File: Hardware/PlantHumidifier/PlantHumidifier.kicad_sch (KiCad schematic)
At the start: 9 parts

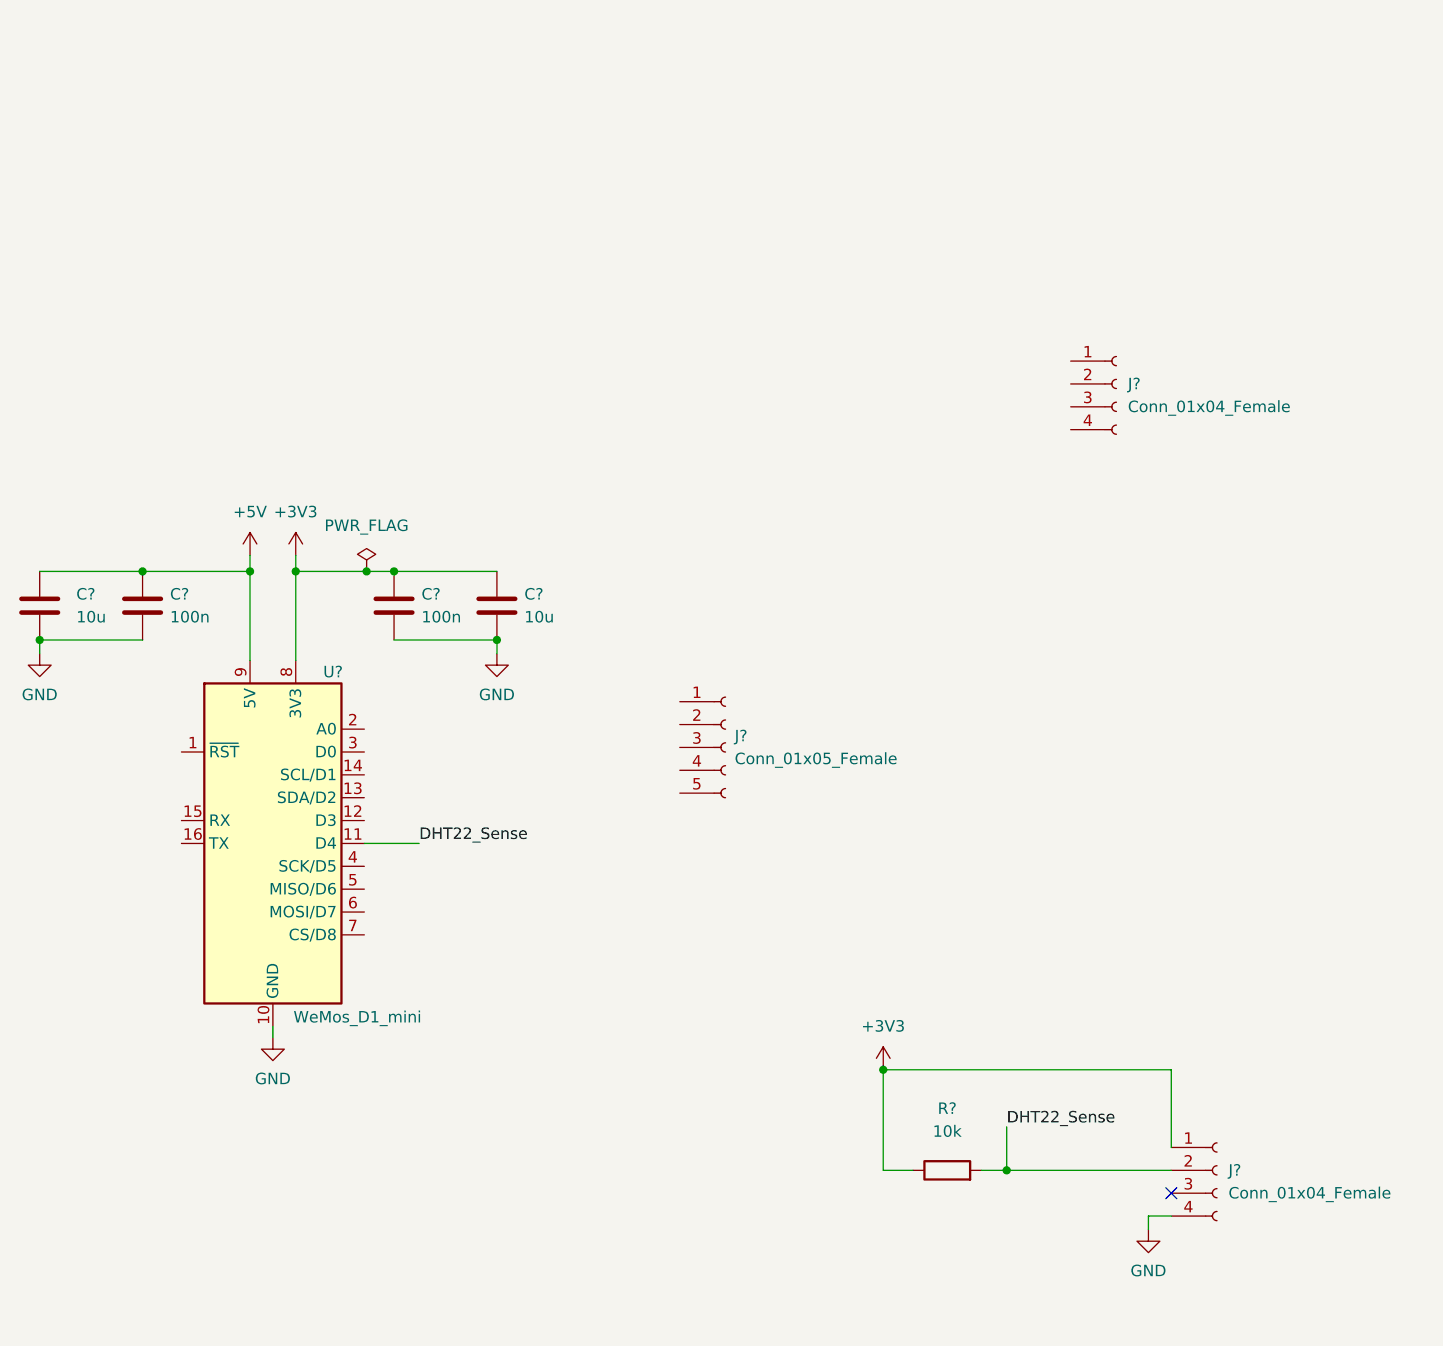
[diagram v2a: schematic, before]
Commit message: Schematic: Wire up OLED screen
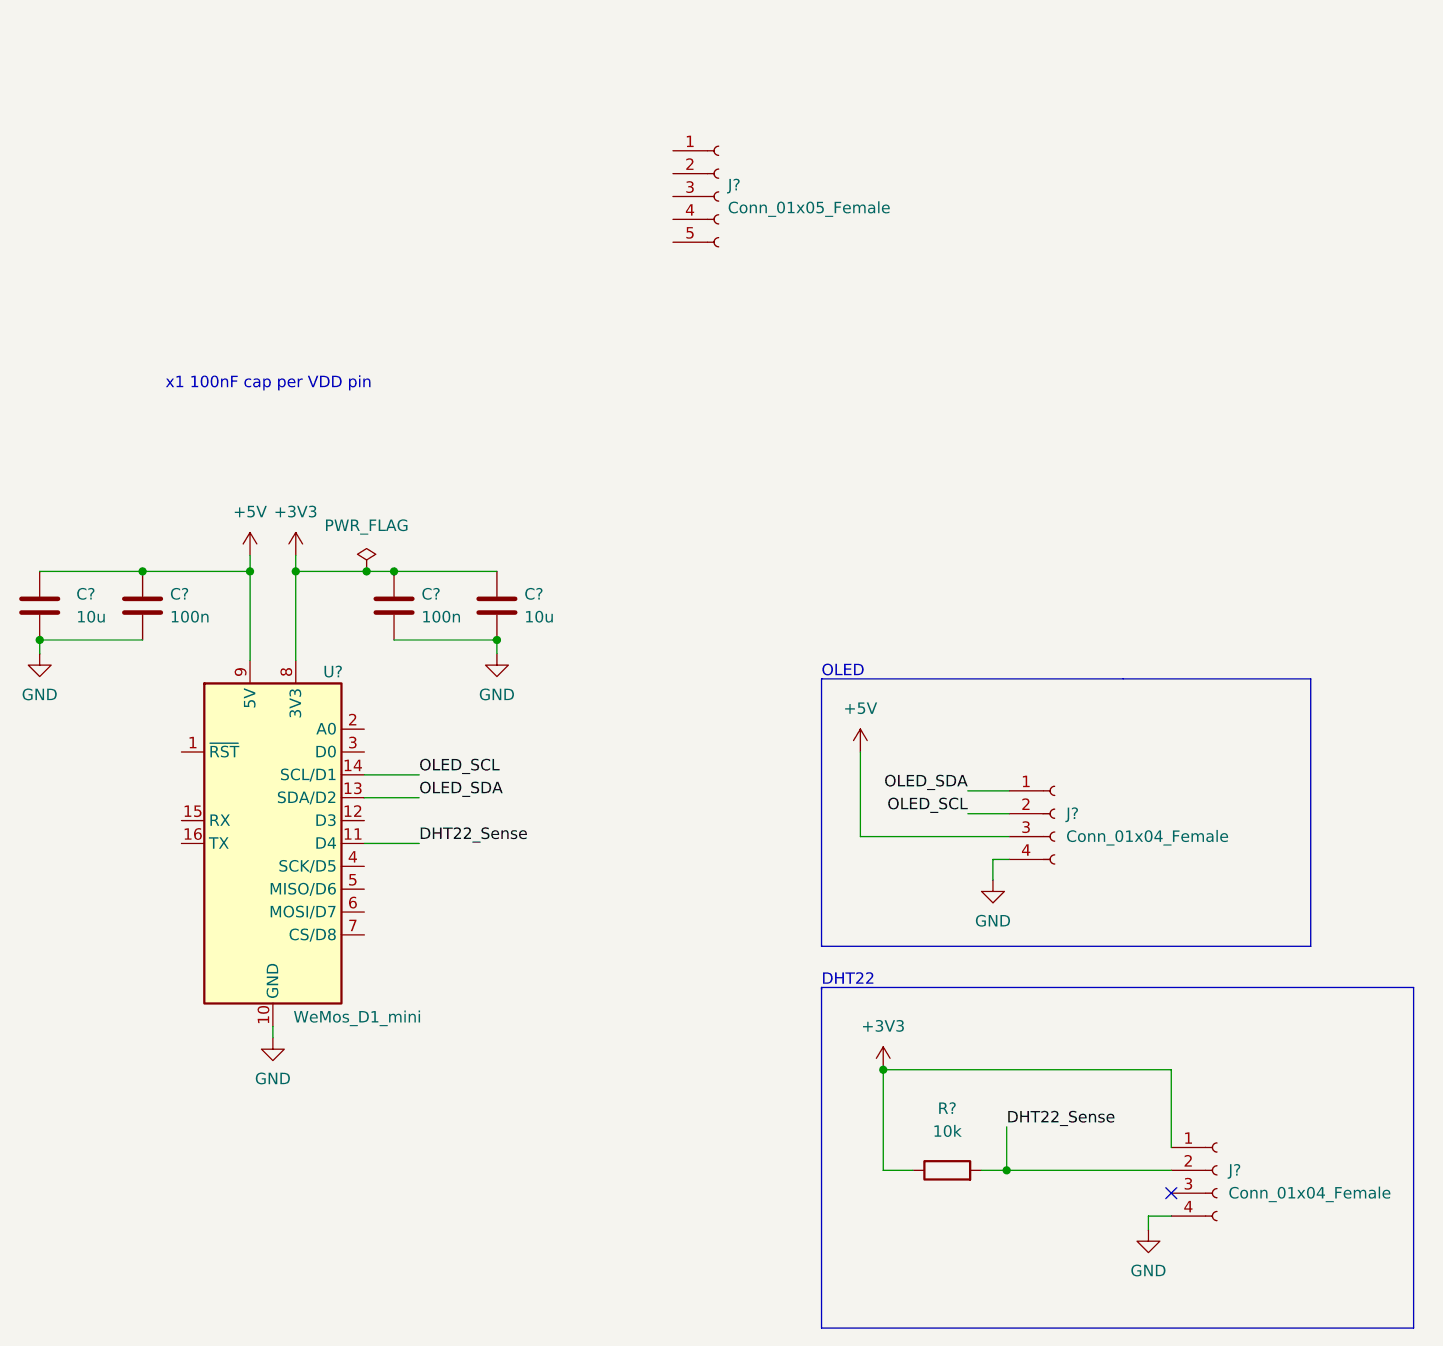
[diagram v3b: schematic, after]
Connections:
- net +5V: now also J?.3 (Pin_3)
- net GND: now also J?.4 (Pin_4)
- net OLED_SDA: now reaches J?.1 (Pin_1)
- net OLED_SDA: now also U?.13 (SDA/D2)
- net OLED_SCL: now reaches J?.2 (Pin_2)
- net OLED_SCL: now also U?.14 (SCL/D1)
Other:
- note added: "DHT22"
- note added: "OLED"
- note added: "x1 100nF cap per VDD pin"
- moved on the sheet: J?
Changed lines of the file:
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@@
+    (stroke (width 0) (type default) (color 0 0 0 0))
+  )
+  (polyline (pts (xy 277.876 123.952) (xy 277.876 161.798))
     (stroke (width 0) (type default) (color 0 0 0 0))
   )
@@
     (stroke (width 0) (type default) (color 0 0 0 0))
   )
+  (polyline (pts (xy 212.09 123.952) (xy 277.876 123.952))
+    (stroke (width 0) (type default) (color 0 0 0 0))
+  )
+  (wire (pts (xy 228.346 104.648) (xy 232.918 104.648))
+    (stroke (width 0) (type default) (color 0 0 0 0))
+  )
+  (polyline (pts (xy 212.09 123.952) (xy 212.09 161.798))
+    (stroke (width 0) (type default) (color 0 0 0 0))
+  )
+  (wire (pts (xy 228.346 102.108) (xy 232.918 102.108))
+    (stroke (width 0) (type default) (color 0 0 0 0))
+  )
+  (polyline (pts (xy 266.446 119.38) (xy 266.446 89.662))
+    (stroke (width 0) (type default) (color 0 0 0 0))
+  )
   (wire (pts (xy 161.544 77.724) (xy 164.592 77.724))
     (stroke (width 0) (type default) (color 0 0 0 0))
@@
     (stroke (width 0) (type default) (color 0 0 0 0))
   )
+  (polyline (pts (xy 277.876 161.798) (xy 212.09 161.798))
+    (stroke (width 0) (type default) (color 0 0 0 0))
+  )
   (wire (pts (xy 164.592 85.344) (xy 176.022 85.344))
     (stroke (width 0) (type default) (color 0 0 0 0))
@@
     (stroke (width 0) (type default) (color 0 0 0 0))
   )
+  (wire (pts (xy 232.918 107.188) (xy 216.408 107.188))
+    (stroke (width 0) (type default) (color 0 0 0 0))
+  )
+  (polyline (pts (xy 212.09 89.662) (xy 212.09 119.38))
+    (stroke (width 0) (type default) (color 0 0 0 0))
+  )
   (wire (pts (xy 148.59 77.724) (xy 148.59 87.63))
     (stroke (width 0) (type default) (color 0 0 0 0))
   )
+  (wire (pts (xy 216.408 97.79) (xy 216.408 107.188))
+    (stroke (width 0) (type default) (color 0 0 0 0))
+  )
   (wire (pts (xy 229.87 144.272) (xy 232.664 144.272))
     (stroke (width 0) (type default) (color 0 0 0 0))
   )
+  (wire (pts (xy 231.14 109.728) (xy 232.918 109.728))
+    (stroke (width 0) (type default) (color 0 0 0 0))
+  )
   (wire (pts (xy 153.67 77.724) (xy 153.67 87.63))
     (stroke (width 0) (type default) (color 0 0 0 0))
@@
     (stroke (width 0) (type default) (color 0 0 0 0))
   )
+  (polyline (pts (xy 245.618 89.662) (xy 212.09 89.662))
+    (stroke (width 0) (type default) (color 0 0 0 0))
+  )
+  (polyline (pts (xy 212.09 123.952) (xy 212.09 124.206))
+    (stroke (width 0) (type default) (color 0 0 0 0))
+  )
   (wire (pts (xy 151.13 128.27) (xy 151.13 129.54))
     (stroke (width 0) (type default) (color 0 0 0 0))
   )
+  (wire (pts (xy 231.14 112.014) (xy 231.14 109.728))
+    (stroke (width 0) (type default) (color 0 0 0 0))
+  )
   (wire (pts (xy 248.412 149.352) (xy 248.412 150.876))
     (stroke (width 0) (type default) (color 0 0 0 0))
@@
     (stroke (width 0) (type default) (color 0 0 0 0))
   )
+  (polyline (pts (xy 212.09 119.38) (xy 266.446 119.38))
+    (stroke (width 0) (type default) (color 0 0 0 0))
+  )
   (wire (pts (xy 250.952 141.732) (xy 250.952 133.096))
     (stroke (width 0) (type default) (color 0 0 0 0))
@@
     (stroke (width 0) (type default) (color 0 0 0 0))
   )
+  (polyline (pts (xy 245.618 89.662) (xy 266.446 89.662))
+    (stroke (width 0) (type default) (color 0 0 0 0))
+  )
   (wire (pts (xy 125.222 77.724) (xy 136.652 77.724))
     (stroke (width 0) (type default) (color 0 0 0 0))
@@
     (stroke (width 0) (type default) (color 0 0 0 0))
   )
+  (wire (pts (xy 161.29 102.87) (xy 167.386 102.87))
+    (stroke (width 0) (type default) (color 0 0 0 0))
+  )
   (wire (pts (xy 218.948 144.272) (xy 222.25 144.272))
     (stroke (width 0) (type default) (color 0 0 0 0))
@@
     (stroke (width 0) (type default) (color 0 0 0 0))
   )
+  (wire (pts (xy 161.29 100.33) (xy 167.386 100.33))
+    (stroke (width 0) (type default) (color 0 0 0 0))
+  )
+  (text "x1 100nF cap per VDD pin" (at 139.192 57.658 0)
+    (effects (font (size 1.27 1.27)) (justify left bottom))
+  )
+  (text "OLED" (at 212.09 89.662 0)
+    (effects (font (size 1.27 1.27)) (justify left bottom))
+  )
+  (text "DHT22" (at 212.09 123.952 0)
+    (effects (font (size 1.27 1.27)) (justify left bottom))
+  )
+  (label "OLED_SDA" (at 167.386 102.87 0)
+    (effects (font (size 1.27 1.27)) (justify left bottom))
+  )
   (label "DHT22_Sense" (at 167.386 107.95 0)
     (effects (font (size 1.27 1.27)) (justify left bottom))
   )
+  (label "OLED_SCL" (at 167.386 100.33 0)
+    (effects (font (size 1.27 1.27)) (justify left bottom))
+  )
+  (label "OLED_SCL" (at 228.346 104.648 180)
+    (effects (font (size 1.27 1.27)) (justify right bottom))
+  )
   (label "DHT22_Sense" (at 232.664 139.446 0)
     (effects (font (size 1.27 1.27)) (justify left bottom))
+  )
+  (label "OLED_SDA" (at 228.346 102.108 180)
+    (effects (font (size 1.27 1.27)) (justify right bottom))
   )
   (symbol (lib_id "Device:C") (at 164.592 81.534 0) (unit 1)
@@
     (pin "1")
   )
-  (symbol (lib_id "Connector:Conn_01x04_Female") (at 244.856 56.896 0) (unit 1)
-    (in_bom yes) (on_board yes) (fields_autoplaced)
-    (property "Reference" "J?" (id 0) (at 246.126 56.8959 0)
-      (effects (font (size 1.27 1.27)) (justify left))
-    )
-    (property "Value" "Conn_01x04_Female" (id 1) (at 246.126 59.4359 0)
-      (effects (font (size 1.27 1.27)) (justify left))
-    )
-    (property "Footprint" "" (id 2) (at 244.856 56.896 0)
-      (effects (font (size 1.27 1.27)) hide)
-    )
-    (property "Datasheet" "~" (id 3) (at 244.856 56.896 0)
+  (symbol (lib_id "Connector:Conn_01x04_Female") (at 237.998 104.648 0) (unit 1)
+    (in_bom yes) (on_board yes) (fields_autoplaced)
+    (property "Reference" "J?" (id 0) (at 239.268 104.6479 0)
+      (effects (font (size 1.27 1.27)) (justify left))
+    )
+    (property "Value" "Conn_01x04_Female" (id 1) (at 239.268 107.1879 0)
+      (effects (font (size 1.27 1.27)) (justify left))
+    )
+    (property "Footprint" "" (id 2) (at 237.998 104.648 0)
+      (effects (font (size 1.27 1.27)) hide)
+    )
+    (property "Datasheet" "~" (id 3) (at 237.998 104.648 0)
       (effects (font (size 1.27 1.27)) hide)
     )
@@
     )
     (property "Datasheet" "" (id 3) (at 148.59 75.946 0)
+      (effects (font (size 1.27 1.27)) hide)
+    )
+    (pin "1")
+  )
+  (symbol (lib_id "power:+5V") (at 216.408 97.79 0) (unit 1)
+    (in_bom yes) (on_board yes) (fields_autoplaced)
+    (property "Reference" "#PWR?" (id 0) (at 216.408 101.6 0)
+      (effects (font (size 1.27 1.27)) hide)
+    )
+    (property "Value" "+5V" (id 1) (at 216.408 92.964 0))
+    (property "Footprint" "" (id 2) (at 216.408 97.79 0)
+      (effects (font (size 1.27 1.27)) hide)
+    )
+    (property "Datasheet" "" (id 3) (at 216.408 97.79 0)
       (effects (font (size 1.27 1.27)) hide)
     )
@@
     (pin "2")
   )
-  (symbol (lib_id "Connector:Conn_01x05_Female") (at 201.422 97.282 0) (unit 1)
-    (in_bom yes) (on_board yes) (fields_autoplaced)
-    (property "Reference" "J?" (id 0) (at 202.438 96.0119 0)
-      (effects (font (size 1.27 1.27)) (justify left))
-    )
-    (property "Value" "Conn_01x05_Female" (id 1) (at 202.438 98.5519 0)
-      (effects (font (size 1.27 1.27)) (justify left))
-    )
-    (property "Footprint" "" (id 2) (at 201.422 97.282 0)
-      (effects (font (size 1.27 1.27)) hide)
-    )
-    (property "Datasheet" "~" (id 3) (at 201.422 97.282 0)
+  (symbol (lib_id "Connector:Conn_01x05_Female") (at 200.66 36.068 0) (unit 1)
+    (in_bom yes) (on_board yes) (fields_autoplaced)
+    (property "Reference" "J?" (id 0) (at 201.676 34.7979 0)
+      (effects (font (size 1.27 1.27)) (justify left))
+    )
+    (property "Value" "Conn_01x05_Female" (id 1) (at 201.676 37.3379 0)
+      (effects (font (size 1.27 1.27)) (justify left))
+    )
+    (property "Footprint" "" (id 2) (at 200.66 36.068 0)
+      (effects (font (size 1.27 1.27)) hide)
+    )
+    (property "Datasheet" "~" (id 3) (at 200.66 36.068 0)
       (effects (font (size 1.27 1.27)) hide)
     )
@@
     (pin "1")
     (pin "2")
+  )
+  (symbol (lib_id "power:GND") (at 231.14 112.014 0) (unit 1)
+    (in_bom yes) (on_board yes) (fields_autoplaced)
+    (property "Reference" "#PWR?" (id 0) (at 231.14 118.364 0)
+      (effects (font (size 1.27 1.27)) hide)
+    )
+    (property "Value" "GND" (id 1) (at 231.14 116.586 0))
+    (property "Footprint" "" (id 2) (at 231.14 112.014 0)
+      (effects (font (size 1.27 1.27)) hide)
+    )
+    (property "Datasheet" "" (id 3) (at 231.14 112.014 0)
+      (effects (font (size 1.27 1.27)) hide)
+    )
+    (pin "1")
   )
   (symbol (lib_id "power:GND") (at 248.412 150.876 0) (unit 1)
@@
       (reference "#PWR?") (unit 1) (value "+5V") (footprint "")
     )
+    (path "/8ccc0a5a-fe0c-46c5-b176-328602079c55"
+      (reference "#PWR?") (unit 1) (value "+5V") (footprint "")
+    )
     (path "/e3933081-4e4f-42b2-bbd3-5138b562a407"
       (reference "#PWR?") (unit 1) (value "+3V3") (footprint "")
     )
+    (path "/ec20d94a-08e8-4671-9a9a-8b62a8e381ba"
+      (reference "#PWR?") (unit 1) (value "GND") (footprint "")
+    )
     (path "/ee81aa02-5bb1-474f-94e6-aba1a34905a6"
